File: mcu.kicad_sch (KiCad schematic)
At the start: 18 parts, among them J11 Conn_ARM_JTAG_SWD_10, SW1 SW_Push, U3 ATSAMD21J18A-A, Y1 Crystal

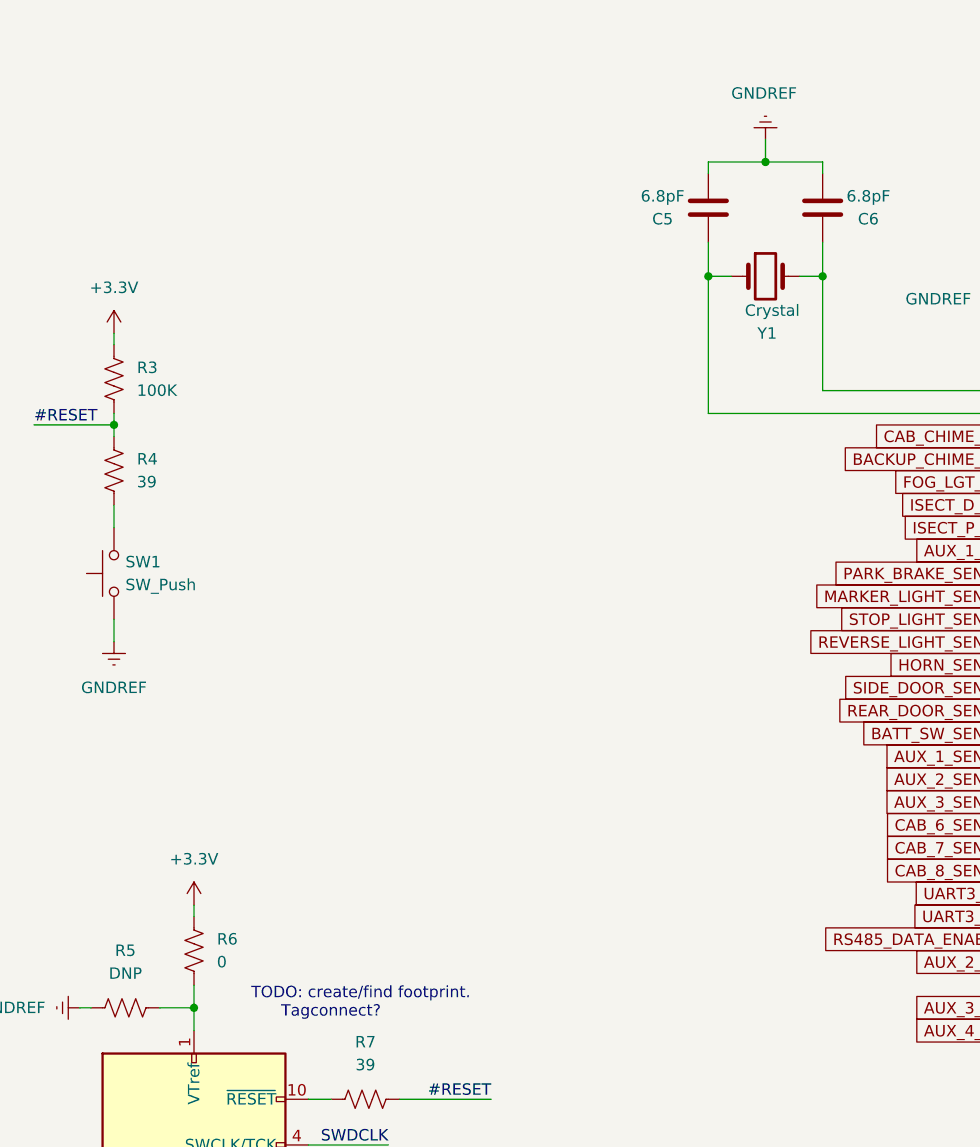
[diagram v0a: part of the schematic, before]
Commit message: begin grouping parts
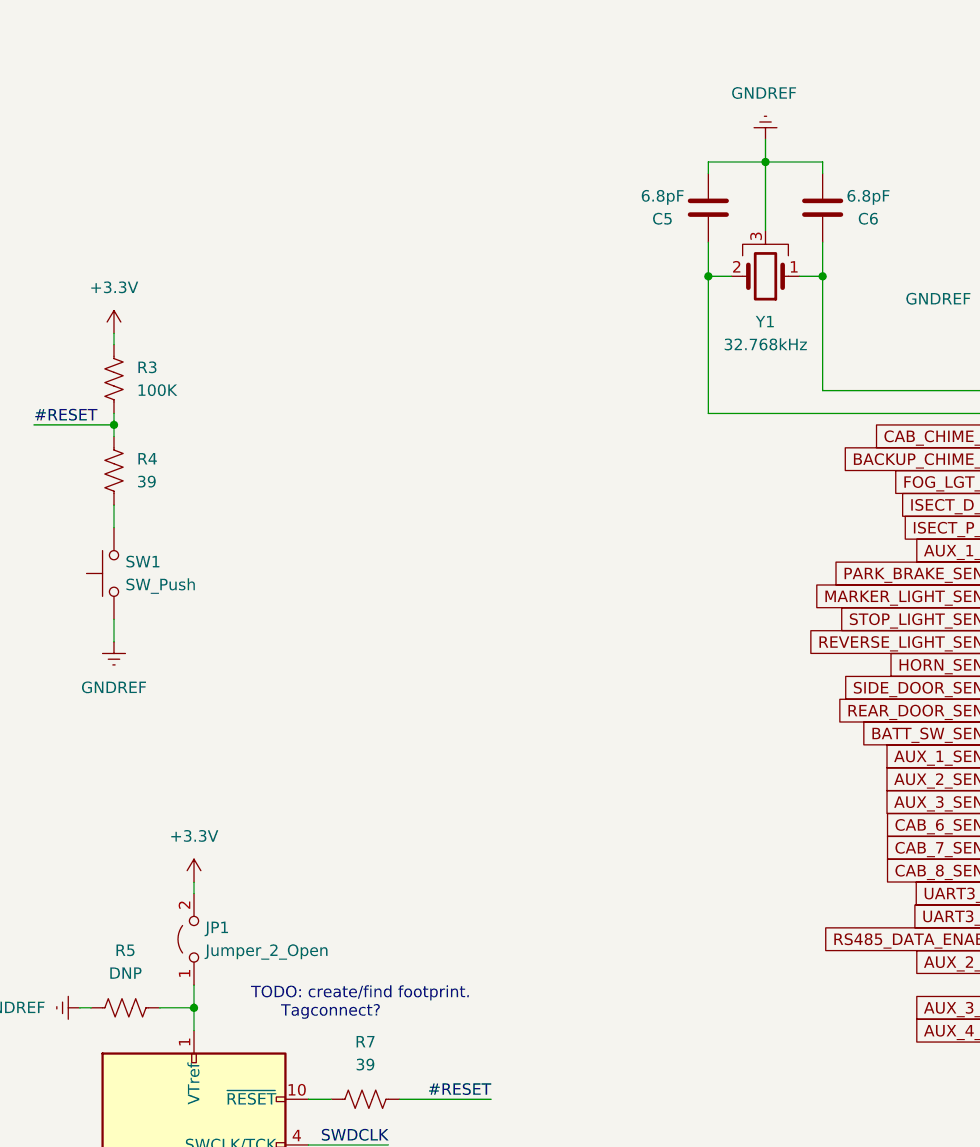
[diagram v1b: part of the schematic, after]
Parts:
- removed R6: 0, Resistor_SMD:R_0805_2012Metric_Pad1.20x1.40mm_HandSolder, symbol Device:R_US
- removed Y1: Crystal, Crystal:Crystal_SMD_MicroCrystal_MS1V-T1K, symbol Device:Crystal
- added JP1: Jumper_2_Open, Connector_PinHeader_2.54mm:PinHeader_1x02_P2.54mm_Vertical, symbol Jumper:Jumper_2_Open
- added Y1: 32.768kHz, Crystal:Crystal_SMD_MicroCrystal_MS1V-T1K, symbol Device:Crystal_GND3
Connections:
- net +3.3V: now also JP1.2 (B)
- net GNDREF: now also Y1.3
- net at J11.1 (VTref), R5.1: now also JP1.1 (A)
- net at C6.2, U3.1 (PA00): now also Y1.1
- net at C5.2, U3.2 (PA01): now also Y1.2
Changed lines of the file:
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@@
+    (stroke (width 0) (type default))
+  )
+  (wire (pts (xy 146.05 36.83) (xy 146.05 44.45))
     (stroke (width 0) (type default))
   )
@@
     (stroke (width 0) (type default))
   )
-  (wire (pts (xy 82.55 119.38) (xy 82.55 120.65))
+  (wire (pts (xy 82.55 116.84) (xy 82.55 118.11))
     (stroke (width 0) (type default))
   )
@@
     )
   )
-  (symbol (lib_id "Device:R_US") (at 82.55 124.46 180) (unit 1)
+  (symbol (lib_id "Jumper:Jumper_2_Open") (at 82.55 123.19 90) (unit 1)
     (in_bom yes) (on_board yes) (dnp no) (fields_autoplaced)
-    (property "Reference" "R6" (at 85.09 123.19 0)
+    (property "Reference" "JP1" (at 83.82 121.92 90)
       (effects (font (size 1.27 1.27)) (justify right))
     )
-    (property "Value" "0" (at 85.09 125.73 0)
+    (property "Value" "Jumper_2_Open" (at 83.82 124.46 90)
       (effects (font (size 1.27 1.27)) (justify right))
     )
-    (property "Footprint" "Resistor_SMD:R_0805_2012Metric_Pad1.20x1.40mm_HandSolder" (at 81.534 124.206 90)
-      (effects (font (size 1.27 1.27)) hide)
-    )
-    (property "Datasheet" "~" (at 82.55 124.46 0)
-      (effects (font (size 1.27 1.27)) hide)
-    )
-    (pin "1")
+    (property "Footprint" "Connector_PinHeader_2.54mm:PinHeader_1x02_P2.54mm_Vertical" (at 82.55 123.19 0)
+      (effects (font (size 1.27 1.27)) hide)
+    )
+    (property "Datasheet" "~" (at 82.55 123.19 0)
+      (effects (font (size 1.27 1.27)) hide)
+    )
     (pin "2")
-    (instances
-      (project "control"
-        (path "/4abb0fa8-15fd-4934-981d-8c1518e957b7/07551e16-8169-4161-b345-aacecb867638"
-          (reference "R6") (unit 1)
+    (pin "1")
+    (instances
+      (project "control"
+        (path "/4abb0fa8-15fd-4934-981d-8c1518e957b7/07551e16-8169-4161-b345-aacecb867638"
+          (reference "JP1") (unit 1)
         )
       )
@@
     )
   )
+  (symbol (lib_id "Device:Crystal_GND3") (at 146.05 49.53 180) (unit 1)
+    (in_bom yes) (on_board yes) (dnp no) (fields_autoplaced)
+    (property "Reference" "Y1" (at 146.05 54.61 0)
+      (effects (font (size 1.27 1.27)))
+    )
+    (property "Value" "32.768kHz" (at 146.05 57.15 0)
+      (effects (font (size 1.27 1.27)))
+    )
+    (property "Footprint" "Crystal:Crystal_SMD_MicroCrystal_MS1V-T1K" (at 146.05 49.53 0)
+      (effects (font (size 1.27 1.27)) hide)
+    )
+    (property "Datasheet" "~" (at 146.05 49.53 0)
+      (effects (font (size 1.27 1.27)) hide)
+    )
+    (pin "1")
+    (pin "2")
+    (pin "3")
+    (instances
+      (project "control"
+        (path "/4abb0fa8-15fd-4934-981d-8c1518e957b7/07551e16-8169-4161-b345-aacecb867638"
+          (reference "Y1") (unit 1)
+        )
+      )
+    )
+  )
   (symbol (lib_id "Device:C") (at 152.4 41.91 0) (mirror y) (unit 1)
     (in_bom yes) (on_board yes) (dnp no)
@@
     )
   )
-  (symbol (lib_id "Device:Crystal") (at 146.05 49.53 0) (unit 1)
-    (in_bom yes) (on_board yes) (dnp no)
-    (property "Reference" "Y1" (at 147.32 55.88 0)
-      (effects (font (size 1.27 1.27)) (justify right))
-    )
-    (property "Value" "Crystal" (at 149.86 53.34 0)
-      (effects (font (size 1.27 1.27)) (justify right))
-    )
-    (property "Footprint" "Crystal:Crystal_SMD_MicroCrystal_MS1V-T1K" (at 146.05 49.53 0)
-      (effects (font (size 1.27 1.27)) hide)
-    )
-    (property "Datasheet" "~" (at 146.05 49.53 0)
-      (effects (font (size 1.27 1.27)) hide)
-    )
-    (pin "1")
-    (pin "2")
-    (instances
-      (project "control"
-        (path "/4abb0fa8-15fd-4934-981d-8c1518e957b7/07551e16-8169-4161-b345-aacecb867638"
-          (reference "Y1") (unit 1)
-        )
-      )
-    )
-  )
-  (symbol (lib_id "power:+3.3V") (at 82.55 119.38 0) (unit 1)
+  (symbol (lib_id "power:+3.3V") (at 82.55 116.84 0) (unit 1)
     (in_bom yes) (on_board yes) (dnp no) (fields_autoplaced)
-    (property "Reference" "#PWR021" (at 82.55 123.19 0)
-      (effects (font (size 1.27 1.27)) hide)
-    )
-    (property "Value" "+3.3V" (at 82.55 114.3 0)
-      (effects (font (size 1.27 1.27)))
-    )
-    (property "Footprint" "" (at 82.55 119.38 0)
-      (effects (font (size 1.27 1.27)) hide)
-    )
-    (property "Datasheet" "" (at 82.55 119.38 0)
-      (effects (font (size 1.27 1.27)) hide)
-    )
+    (property "Reference" "#PWR021" (at 82.55 120.65 0)
+      (effects (font (size 1.27 1.27)) hide)
+    )
+    (property "Value" "+3.3V" (at 82.55 111.76 0)
+      (effects (font (size 1.27 1.27)))
+    )
+    (property "Footprint" "" (at 82.55 116.84 0)
+      (effects (font (size 1.27 1.27)) hide)
+    )
+    (property "Datasheet" "" (at 82.55 116.84 0)
+      (effects (font (size 1.27 1.27)) hide)
+    )

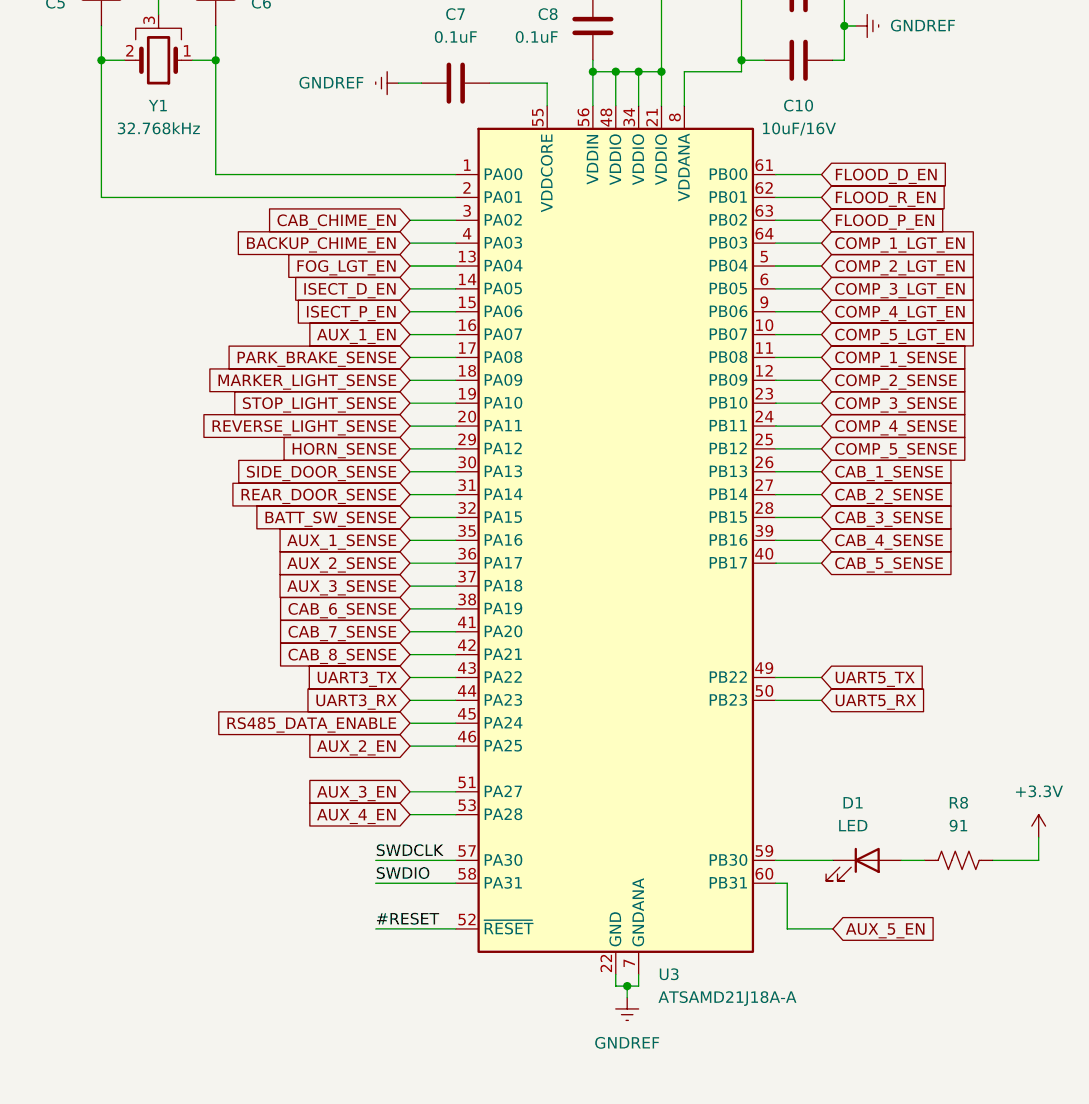
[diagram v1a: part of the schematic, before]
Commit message: lay pre-autorouting tracks
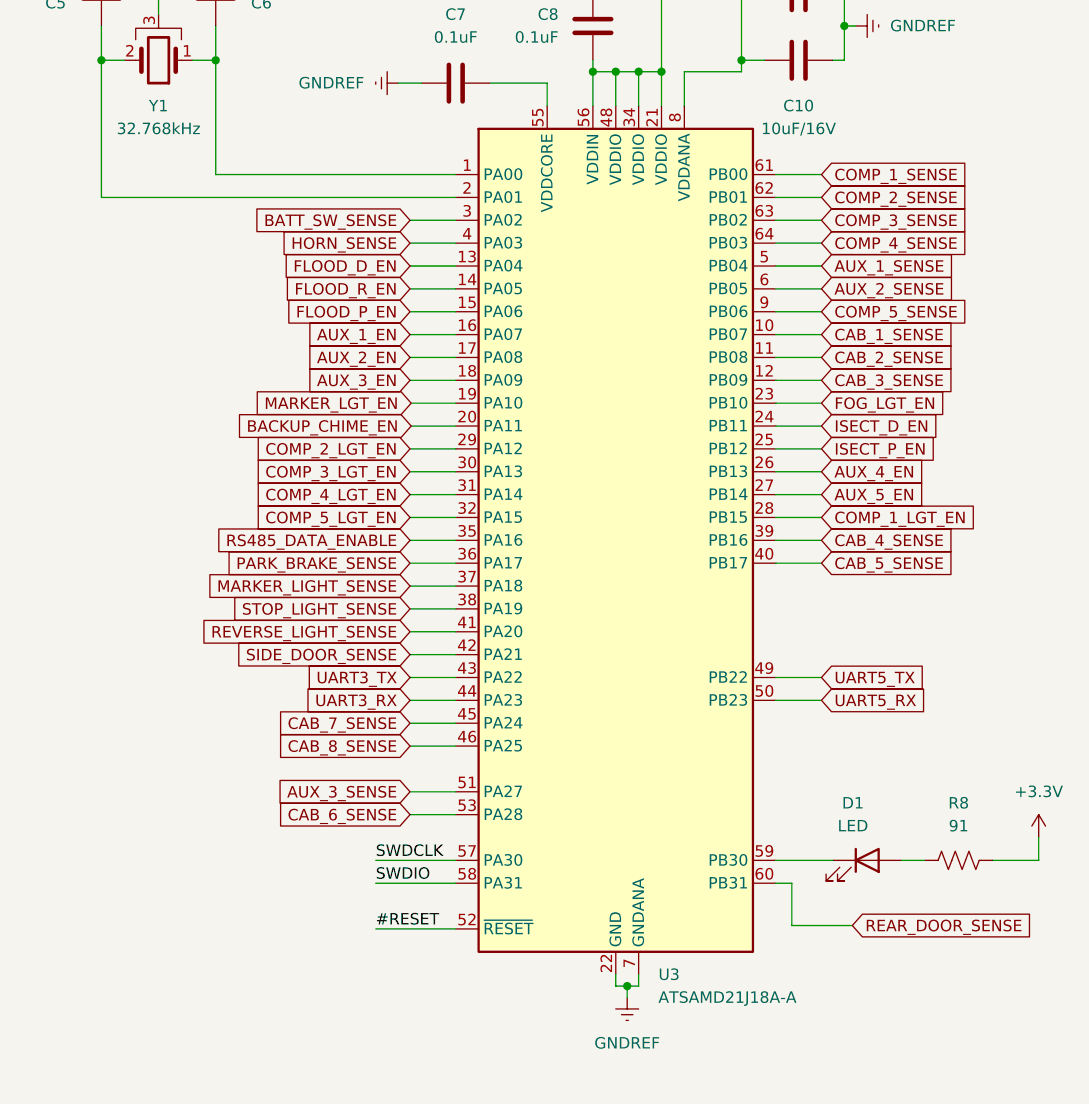
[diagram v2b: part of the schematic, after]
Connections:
- net CAB_CHIME_EN is gone; now on net BATT_SW_SENSE: U3.3 (PA02)
- net AUX_1_SENSE: now also U3.5 (PB04); no longer U3.35 (PA16)
- net AUX_2_EN: now also U3.17 (PA08); no longer U3.46 (PA25)
- net AUX_2_SENSE: now also U3.6 (PB05); no longer U3.36 (PA17)
- net AUX_3_EN: now also U3.18 (PA09); no longer U3.51 (PA27)
- net AUX_3_SENSE: now also U3.51 (PA27); no longer U3.37 (PA18)
- net AUX_4_EN: now also U3.26 (PB13); no longer U3.53 (PA28)
- net AUX_5_EN: now also U3.27 (PB14); no longer U3.60 (PB31)
- net BACKUP_CHIME_EN: now also U3.20 (PA11); no longer U3.4 (PA03)
- net BATT_SW_SENSE: no longer U3.32 (PA15)
- net CAB_1_SENSE: now also U3.10 (PB07); no longer U3.26 (PB13)
- net CAB_2_SENSE: now also U3.11 (PB08); no longer U3.27 (PB14)
- net CAB_3_SENSE: now also U3.12 (PB09); no longer U3.28 (PB15)
- net CAB_6_SENSE: now also U3.53 (PA28); no longer U3.38 (PA19)
- net CAB_7_SENSE: now also U3.45 (PA24); no longer U3.41 (PA20)
- net CAB_8_SENSE: now also U3.46 (PA25); no longer U3.42 (PA21)
- net COMP_1_LGT_EN: now also U3.28 (PB15); no longer U3.64 (PB03)
- net COMP_1_SENSE: now also U3.61 (PB00); no longer U3.11 (PB08)
- net COMP_2_LGT_EN: now also U3.29 (PA12); no longer U3.5 (PB04)
- net COMP_2_SENSE: now also U3.62 (PB01); no longer U3.12 (PB09)
- net COMP_3_LGT_EN: now also U3.30 (PA13); no longer U3.6 (PB05)
- net COMP_3_SENSE: now also U3.63 (PB02); no longer U3.23 (PB10)
- net COMP_4_LGT_EN: now also U3.31 (PA14); no longer U3.9 (PB06)
- net COMP_4_SENSE: now also U3.64 (PB03); no longer U3.24 (PB11)
- net COMP_5_LGT_EN: now also U3.32 (PA15); no longer U3.10 (PB07)
- net COMP_5_SENSE: now also U3.9 (PB06); no longer U3.25 (PB12)
- net FLOOD_D_EN: now also U3.13 (PA04); no longer U3.61 (PB00)
- net FLOOD_P_EN: now also U3.15 (PA06); no longer U3.63 (PB02)
- net FLOOD_R_EN: now also U3.14 (PA05); no longer U3.62 (PB01)
- net FOG_LGT_EN: now also U3.23 (PB10); no longer U3.13 (PA04)
- net HORN_SENSE: now also U3.4 (PA03); no longer U3.29 (PA12)
- net ISECT_D_EN: now also U3.24 (PB11); no longer U3.14 (PA05)
- net ISECT_P_EN: now also U3.25 (PB12); no longer U3.15 (PA06)
- net MARKER_LIGHT_SENSE: now also U3.37 (PA18); no longer U3.18 (PA09)
- net PARK_BRAKE_SENSE: now also U3.36 (PA17); no longer U3.17 (PA08)
- net REAR_DOOR_SENSE: now also U3.60 (PB31); no longer U3.31 (PA14)
- net REVERSE_LIGHT_SENSE: now also U3.41 (PA20); no longer U3.20 (PA11)
- net RS485_DATA_ENABLE: now also U3.35 (PA16); no longer U3.45 (PA24)
- net SIDE_DOOR_SENSE: now also U3.42 (PA21); no longer U3.30 (PA13)
- net STOP_LIGHT_SENSE: now also U3.38 (PA19); no longer U3.19 (PA10)
- new net MARKER_LGT_EN: U3.19 (PA10)
